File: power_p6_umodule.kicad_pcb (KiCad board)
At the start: 4 copper layers, 44.8 x 41.5 mm, 23 parts, among them J1 LSHM-140-04.0-L-DV-A-N-K-TR, U1 LTM4653EY

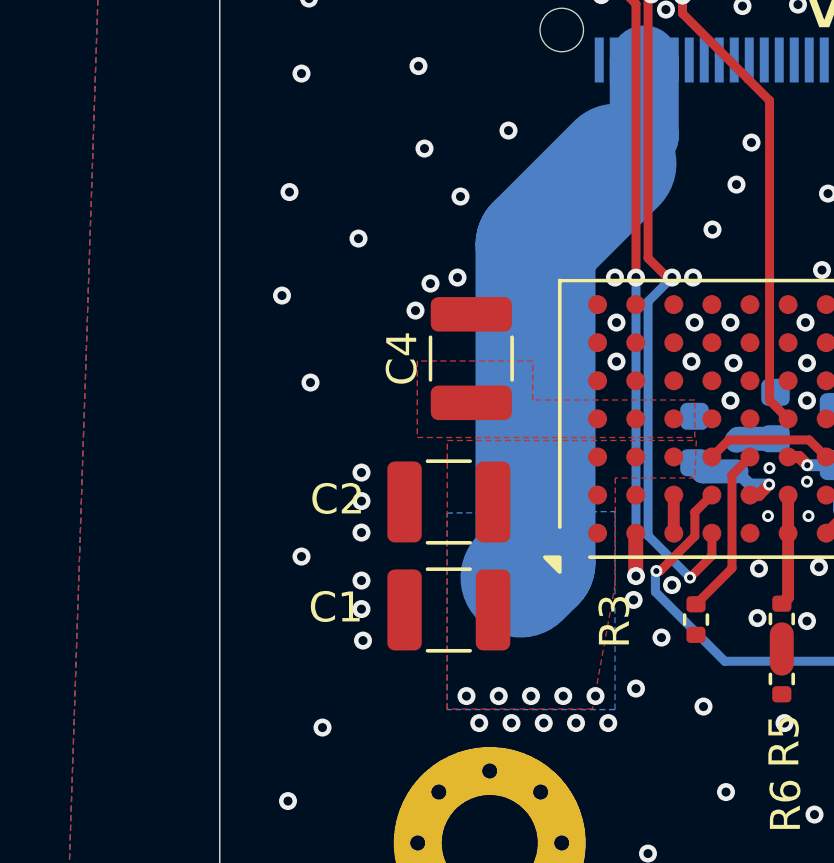
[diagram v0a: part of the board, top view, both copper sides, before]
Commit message: Add input RC snubber
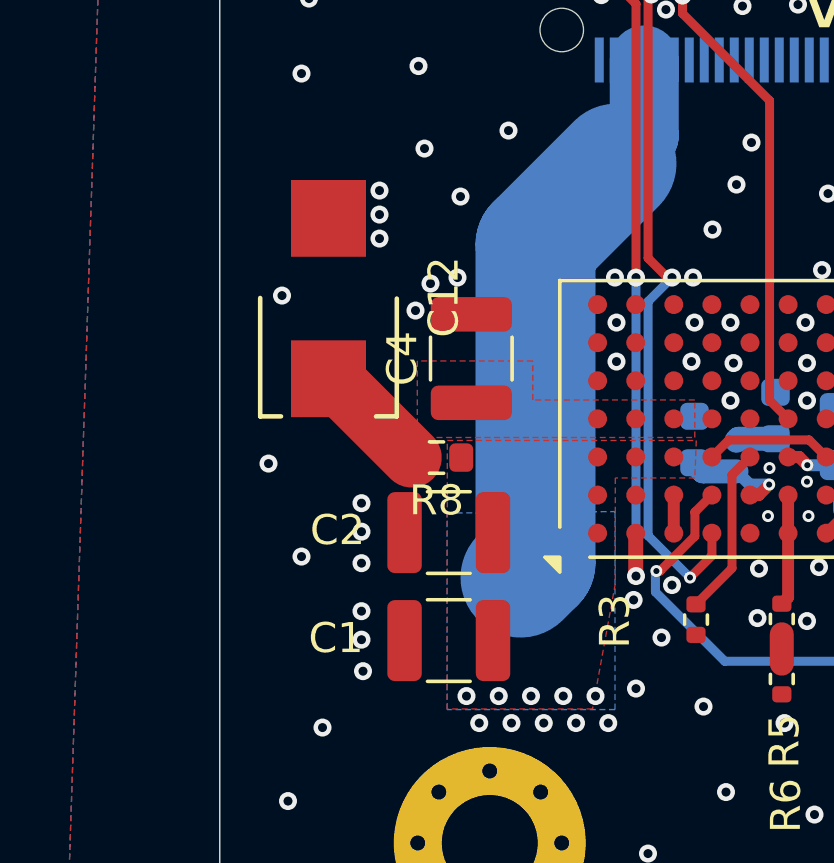
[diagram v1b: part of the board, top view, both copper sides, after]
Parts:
- added C12: 100u, lib:T521X, F.Cu at (106.4, 61.2)
- added R8: 0.5, Resistor_SMD:R_0603_1608Metric, F.Cu at (110.0, 66.5)
- moved C1 1.02 mm to (110.4, 72.6)
- moved C2 1.02 mm to (110.4, 69.0)
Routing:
- net /cf1: track 0.00 -> 3.86 mm
- net GND: vias 174 -> 175
